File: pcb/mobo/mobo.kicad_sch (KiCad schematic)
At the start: 66 parts, among them J1 SWD_10, J2 PEEL_MOTOR, J3 DRIVE_MOTOR, J4 SW1, J5 SPRING_FINGERS, J6 SW2, J7 SW1, J8 USART1, J9 SWD_10, U1 STM32F031C6Tx, U2 STM32F031K6Ux, U4 AP1117-33, U5 MC34063AD, U6 MAX3078E, U7 DRV8837, U8 DRV8837, Y1 8MHz

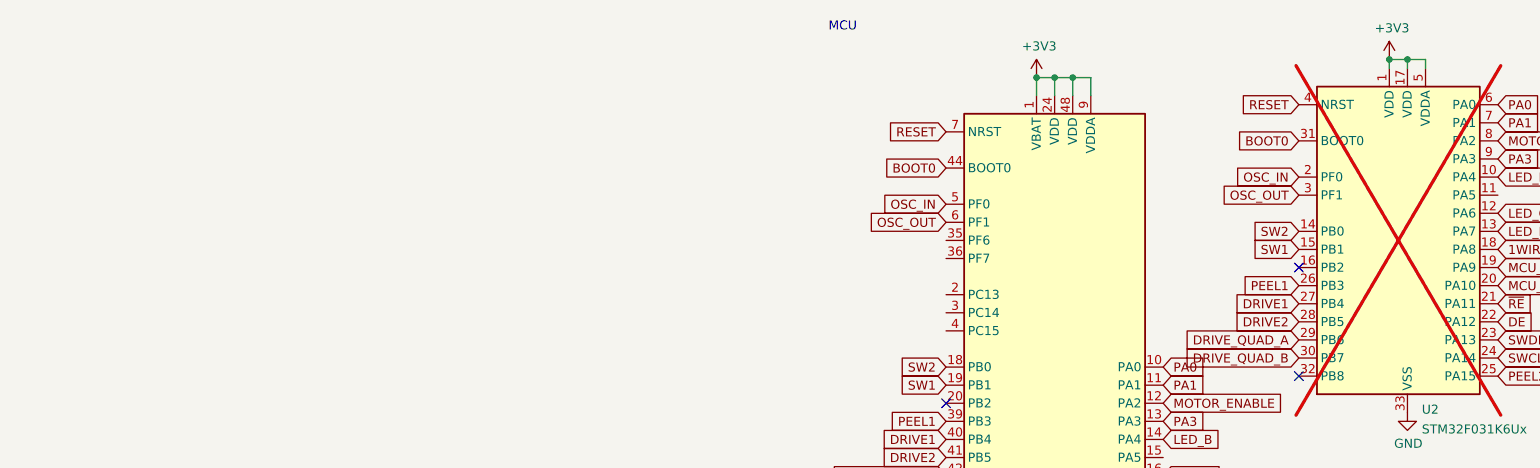
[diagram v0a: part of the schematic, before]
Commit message: Invalid LCSC part for crystal, changed to C527077
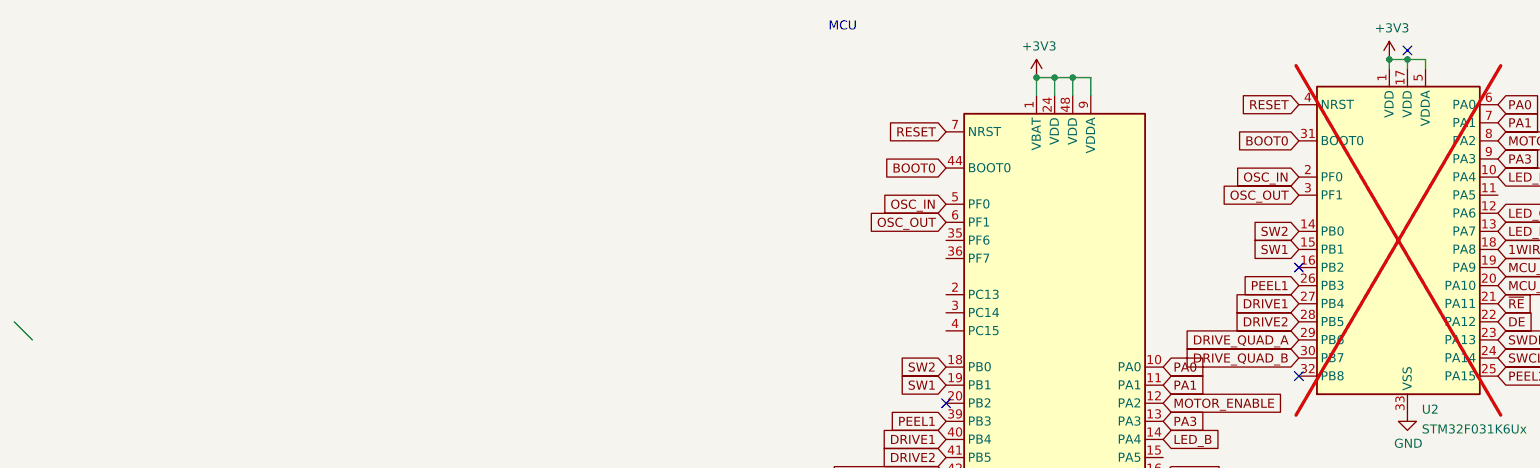
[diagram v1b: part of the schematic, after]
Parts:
- Y1: LCSC C115962 -> C7294546
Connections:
- no-connect marks 8 -> 9
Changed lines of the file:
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@@
 	)
 	(no_connect
+		(at 93.98 17.78)
+	)
+	(no_connect
 		(at 78.74 63.5)
 	)
@@
 		(at 165.1 91.44)
 	)
+	(bus_entry
+		(at -101.6 55.88)
+		(size 2.54 2.54)
+		(stroke
+			(width 0)
+			(type default)
+		)
+	)
 	(wire
 		(pts
@@
 			)
 		)
-		(property "LCSC" "C115962"
+		(property "LCSC" "C7294546"
 			(at 130.81 36.83 0)
 			(effects
@@
 			)
 		)
+		(property "Notes" ""
+			(at 130.81 36.83 0)
+			(effects
+				(font
+					(size 1.27 1.27)
+				)
+				(hide yes)
+			)
+		)
 		(pin "1"
 		)
@@
 			(at 152.4 36.83 0)
 			(effects
+				(font
+					(size 1.27 1.27)
+				)
+				(hide yes)
+			)
+		)
+		(property "DigiKey" ""
+			(at 152.4 36.83 0)
+			(effects

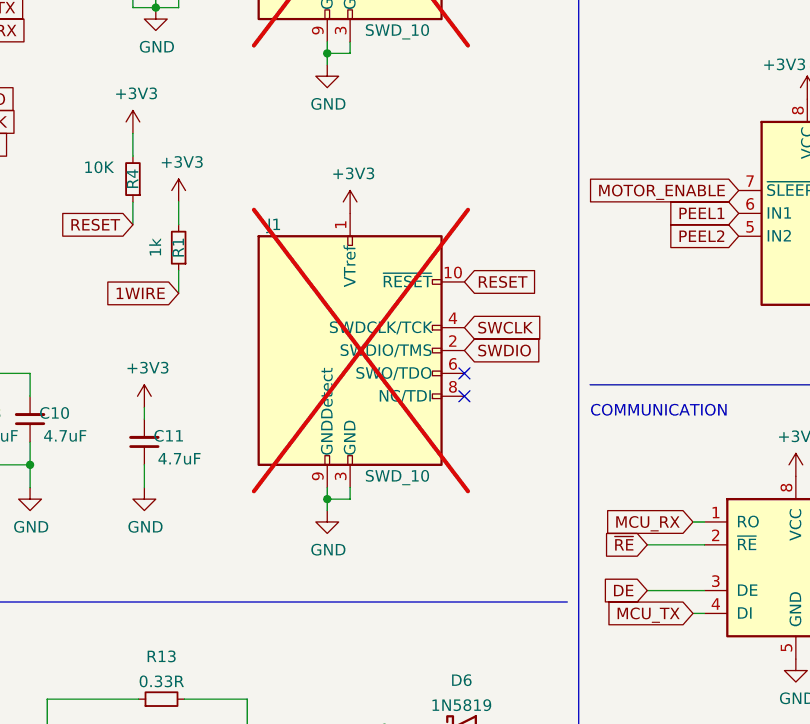
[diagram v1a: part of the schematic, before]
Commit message: Convert SWD connector on back to TC2030. Left one on front for Adafruit 5434 connector.
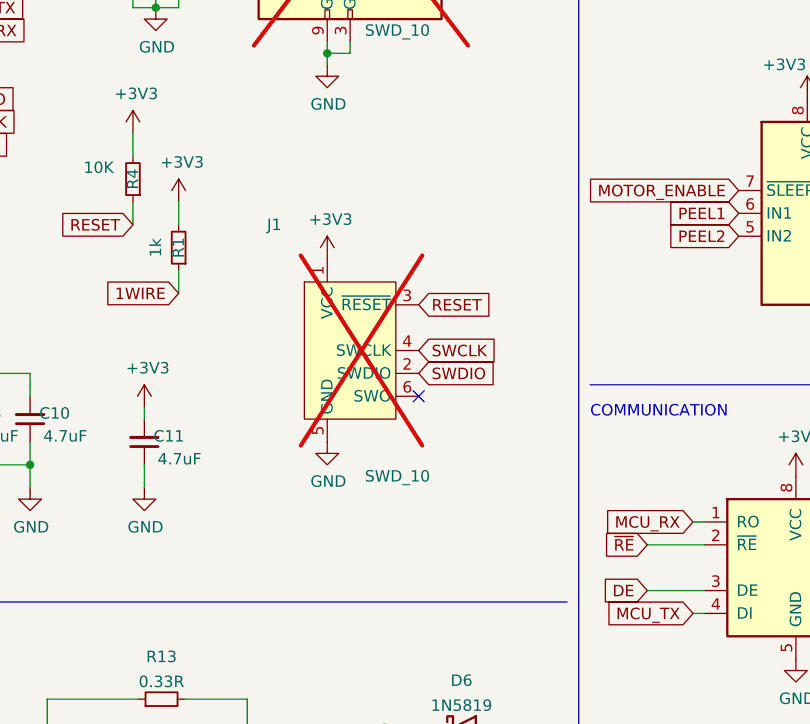
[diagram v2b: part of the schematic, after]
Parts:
- J1: footprint Connector_PinHeader_1.27mm:PinHeader_2x05_P1.27mm_Vertical_SMD -> Connector:Tag-Connect_TC2030-IDC-FP_2x03_P1.27mm_Vertical; symbol Connector:Conn_ARM_JTAG_SWD_10 -> Connector:Conn_ARM_SWD_TagConnect_TC2030; now left out of the parts list
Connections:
- net GND: no longer J1.3 (GND), J1.9 (GNDDetect)
- net RESET: now also J1.3 (~{RESET}); no longer J1.10 (~{RESET})
- no-connect marks 9 -> 8
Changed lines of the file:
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@@
 	)
 	(junction
-		(at 149.86 102.87)
-		(diameter 0)
-		(color 0 0 0 0)
-	)
-	(junction
 		(at 74.93 88.9)
 		(diameter 0)
@@
 	)
 	(no_connect
-		(at 165.1 88.9)
-	)
-	(no_connect
-		(at 165.1 91.44)
+		(at 160.02 91.44)
 	)
 	(bus_entry
@@
 	(wire
 		(pts
-			(xy 152.4 102.87) (xy 152.4 101.6)
-		)
-		(stroke
-			(width 0)
-			(type default)
-		)
-	)
-	(wire
-		(pts
 			(xy 140.97 140.97) (xy 143.51 140.97)
 		)
@@
 	(wire
 		(pts
-			(xy 149.86 102.87) (xy 149.86 101.6)
-		)
-		(stroke
-			(width 0)
-			(type default)
-		)
-	)
-	(wire
-		(pts
 			(xy 109.22 96.52) (xy 109.22 99.06)
 		)
@@
 	(wire
 		(pts
-			(xy 149.86 102.87) (xy 152.4 102.87)
-		)
-		(stroke
-			(width 0)
-			(type default)
-		)
-	)
-	(wire
-		(pts
 			(xy 78.74 180.34) (xy 81.28 180.34)
 		)
@@
 	(wire
 		(pts
-			(xy 149.86 104.14) (xy 149.86 102.87)
-		)
-		(stroke
-			(width 0)
-			(type default)
-		)
-	)
-	(wire
-		(pts
 			(xy 38.1 157.48) (xy 38.1 162.56)
 		)
@@
 	(global_label "SWCLK"
 		(shape input)
-		(at 165.1 83.82 0)
+		(at 160.02 86.36 0)
 		(fields_autoplaced yes)
 		(effects
@@
 		)
 		(property "Intersheetrefs" "${INTERSHEET_REFS}"
-			(at 121.285 1.905 0)
+			(at 116.205 4.445 0)
 			(effects
 				(font
@@
 	(global_label "SWDIO"
 		(shape input)
-		(at 165.1 86.36 0)
+		(at 160.02 88.9 0)
 		(fields_autoplaced yes)
 		(effects
@@
 		)
 		(property "Intersheetrefs" "${INTERSHEET_REFS}"
-			(at 121.285 1.905 0)
+			(at 116.205 4.445 0)
 			(effects
 				(font
@@
 	(global_label "RESET"
 		(shape input)
-		(at 165.1 78.74 0)
+		(at 160.02 81.28 0)
 		(fields_autoplaced yes)
 		(effects
@@
 		)
 		(property "Intersheetrefs" "${INTERSHEET_REFS}"
-			(at 121.285 1.905 0)
+			(at 116.205 4.445 0)
 			(effects
 				(font
@@
 	(symbol
 		(lib_id "power:GND")
-		(at 149.86 104.14 0)
+		(at 149.86 96.52 0)
 		(unit 1)
 		(exclude_from_sim no)
@@
 		(dnp no)
 		(property "Reference" "#PWR04"
-			(at 149.86 110.49 0)
+			(at 149.86 102.87 0)
 			(effects
 				(font
@@
 		)
 		(property "Value" "GND"
-			(at 149.987 108.5342 0)
+			(at 149.987 100.9142 0)
 			(effects
 				(font
@@
 		)
 		(property "Footprint" ""
-			(at 149.86 104.14 0)
+			(at 149.86 96.52 0)
 			(effects
 				(font
@@
 		)
 		(property "Datasheet" ""
-			(at 149.86 104.14 0)
+			(at 149.86 96.52 0)
 			(effects
 				(font
@@
 		)
 		(property "Description" ""
-			(at 149.86 104.14 0)
+			(at 149.86 96.52 0)
 			(effects
 				(font
@@
 	(symbol
 		(lib_id "power:+3V3")
-		(at 152.4 71.12 0)
+		(at 149.86 76.2 0)
 		(unit 1)
 		(exclude_from_sim no)
@@
 		(dnp no)
 		(property "Reference" "#PWR05"
-			(at 152.4 74.93 0)
+			(at 149.86 80.01 0)
 			(effects
 				(font
@@
 		)
 		(property "Value" "+3V3"
-			(at 152.781 66.7258 0)
+			(at 150.241 71.8058 0)
 			(effects
 				(font
@@
 		)
 		(property "Footprint" ""
-			(at 152.4 71.12 0)
+			(at 149.86 76.2 0)
 			(effects
 				(font
@@
 		)
 		(property "Datasheet" ""
-			(at 152.4 71.12 0)
+			(at 149.86 76.2 0)
 			(effects
 				(font
@@
 		)
 		(property "Description" ""
-			(at 152.4 71.12 0)
+			(at 149.86 76.2 0)
 			(effects
 				(font
@@
 	)
 	(symbol
-		(lib_id "Connector:Conn_ARM_JTAG_SWD_10")
+		(lib_id "Connector:Conn_ARM_SWD_TagConnect_TC2030")
 		(at 152.4 86.36 0)
 		(unit 1)
 		(exclude_from_sim no)
-		(in_bom yes)
+		(in_bom no)
 		(on_board yes)
 		(dnp yes)
@@
 			)
 		)
-		(property "Footprint" "Connector_PinHeader_1.27mm:PinHeader_2x05_P1.27mm_Vertical_SMD"
-			(at 152.4 86.36 0)
+		(property "Footprint" "Connector:Tag-Connect_TC2030-IDC-FP_2x03_P1.27mm_Vertical"
+			(at 152.4 104.14 0)
 			(effects
 				(font
@@
 			)
 		)
-		(property "Datasheet" "http://infocenter.arm.com/help/topic/com.arm.doc.ddi0314h/DDI0314H_coresight_components_trm.pdf"
-			(at 143.51 118.11 90)
+		(property "Datasheet" "https://www.tag-connect.com/wp-content/uploads/bsk-pdf-manager/TC2030-CTX_1.pdf"
+			(at 152.4 101.6 0)
 			(effects
 				(font
@@
 			)
 		)
-		(property "Description" ""
+		(property "Description" "Tag-Connect ARM Cortex SWD JTAG connector, 6 pin"
 			(at 152.4 86.36 0)
 			(effects
@@
 			)
 		)
-		(pin "1"
+		(property "LCSC" ""
+			(at 152.4 86.36 0)
+			(effects
+				(font
+					(size 1.27 1.27)
+				)
+				(hide yes)
+			)
 		)
-		(pin "10"
+		(property "DigiKey" ""
+			(at 152.4 86.36 0)
+			(effects
+				(font
+					(size 1.27 1.27)
+				)
+				(hide yes)
+			)
+		)
+		(property "Mouser" ""
+			(at 152.4 86.36 0)
+			(effects
+				(font
+					(size 1.27 1.27)
+				)
+				(hide yes)
+			)
+		)
+		(pin "1"
 		)
 		(pin "2"
@@
 		(pin "6"
 		)
-		(pin "7"
-		)
-		(pin "8"
-		)
-		(pin "9"
-		)
 		(instances
 			(project "mobo"
@@
 			(at 152.4 36.83 0)
 			(effects
+				(font
+					(size 1.27 1.27)
+				)
+				(hide yes)
+			)
+		)
+		(property "LCSC" ""
+			(at 152.4 36.83 0)
+			(effects
+				(font
+					(size 1.27 1.27)
+				)
+				(hide yes)
+			)
+		)
+		(property "Mouser" ""
+			(at 152.4 36.83 0)
+			(effects

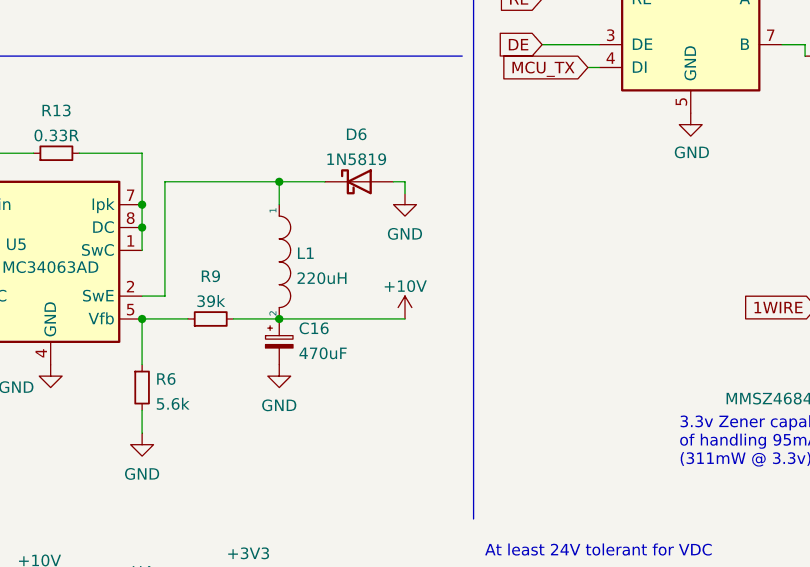
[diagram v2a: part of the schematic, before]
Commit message: Modify SWD footprint to make compatible with Adafruit 5434
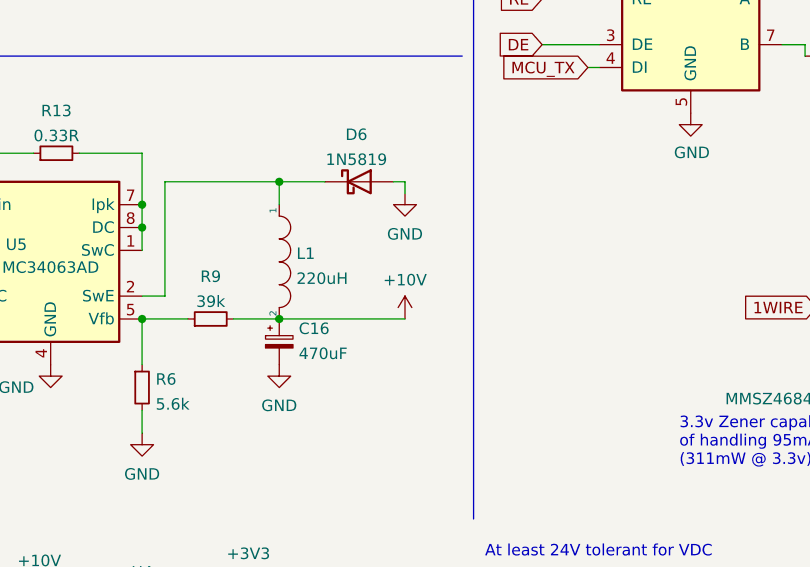
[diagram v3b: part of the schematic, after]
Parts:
- C12: DigiKey 565-EMZR500ARA101MF80GCT-ND -> PCE3951CT-ND; LCSC C962164 -> C178512; Mouser 661-EMZR500ARA101MF8 -> 667-EEE-1VA101XP
- D6: footprint Diode_SMD:D_SOD-123 -> Diode_SMD:D_SOD-323_HandSoldering; LCSC C963381 -> C191023
- J2: DigiKey WM1746-ND -> WM7620CT-ND; Mouser 538-53048-0610 -> 53261-0271; Notes MouserAlt: 53261-0671; DigiKeyAlt: WM7624CT-ND -> Order cable ‎0151340201, it's female to female 100mm. Cut i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
- J3: Notes MouserAlt: 53261-0671; DigiKeyAlt: WM7624CT-ND -> (none)
- J9: DigiKey (none) -> 1528-5434-ND; Mouser (none) -> 485-5434; Notes WARNING: Is there room in the model for this -> Adafruit 5434 compatible; now left out of the parts list
- Y1: LCSC C7294546 -> C5308002
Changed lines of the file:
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@@
 			)
 		)
-		(property "LCSC" "C7294546"
+		(property "LCSC" "C5308002"
 			(at 130.81 36.83 0)
 			(effects
@@
 			)
 		)
+		(property "Notes" ""
+			(at 201.93 110.49 0)
+			(effects
+				(font
+					(size 1.27 1.27)
+				)
+				(hide yes)
+			)
+		)
 		(pin "1"
 		)
@@
 		(unit 1)
 		(exclude_from_sim no)
-		(in_bom yes)
+		(in_bom no)
 		(on_board yes)
 		(dnp yes)
@@
 			)
 		)
-		(property "Description" ""
+		(property "Description" "2x5p 1.27mm Pogo"
 			(at 152.4 36.83 0)
 			(effects
@@
 			)
 		)
-		(property "Notes" "WARNING: Is there room in the model for this"
+		(property "Notes" "Adafruit 5434 compatible"
 			(at 152.4 36.83 0)
 			(effects
@@
 			)
 		)
-		(property "DigiKey" ""
+		(property "DigiKey" "1528-5434-ND"
 			(at 152.4 36.83 0)
 			(effects
@@
 			)
 		)
-		(property "Mouser" ""
+		(property "Mouser" "485-5434"
 			(at 152.4 36.83 0)
 			(effects
@@
 			)
 		)
-		(property "Description" ""
+		(property "Description" "100V X5R"
 			(at 116.84 144.78 0)
 			(effects
@@
 			)
 		)
-		(property "Footprint" "Diode_SMD:D_SOD-123"
+		(property "Footprint" "Diode_SMD:D_SOD-323_HandSoldering"
 			(at 165.1 132.715 0)
 			(effects
@@
 			)
 		)
-		(property "LCSC" "C963381"
+		(property "LCSC" "C191023"
 			(at 165.1 128.27 0)
 			(effects
@@
 			)
 		)
+		(property "Notes" ""
+			(at 165.1 128.27 0)
+			(effects
+				(font
+					(size 1.27 1.27)
+				)
+				(hide yes)
+			)
+		)
 		(pin "1"
 		)
@@
 			)
 		)
-		(property "Description" "PicoBlade 1x6 right-angle Header"
+		(property "Description" "PicoBlade 1x2 right-angle Header"
 			(at 234.95 73.66 0)
 			(effects
@@
 			)
 		)
-		(property "DigiKey" "WM1746-ND"
+		(property "DigiKey" "WM7620CT-ND"
 			(at 234.95 73.66 0)
 			(effects
@@
 			)
 		)
-		(property "Mouser" "538-53048-0610"
+		(property "Mouser" "53261-0271"
 			(at 234.95 73.66 0)
 			(effects
@@
 			)
 		)
-		(property "Notes" "MouserAlt: 53261-0671; DigiKeyAlt: WM7624CT-ND"
+		(property "Notes" "Order cable ‎0151340201, it's female to female 100mm. Cut in half, makes two peel motor pigtails"
 			(at 234.95 73.66 0)
 			(effects
@@
 		(on_board yes)
 		(dnp no)
-		(fields_autoplaced yes)
 		(property "Reference" "#PWR0114"
 			(at 170.18 147.32 0)
@@
 		)
 		(property "Value" "+10V"
-			(at 170.18 139.9055 0)
+			(at 170.18 139.192 0)
 			(effects
 				(font
@@
 			)
 		)
-		(property "Notes" "MouserAlt: 53261-0671; DigiKeyAlt: WM7624CT-ND"
+		(property "Notes" ""
 			(at 242.57 27.94 0)
 			(effects
@@
 			)
 		)
-		(property "Description" "100uf 50V 2000H@105c ±20%"
+		(property "Description" "100uf 35V 2000H@105c ±20%"
 			(at 110.49 133.35 0)
 			(effects
@@
 			)
 		)
-		(property "LCSC" "C962164"
+		(property "LCSC" "C178512"
 			(at 110.49 133.35 0)
 			(effects
@@
 			)
 		)
-		(property "DigiKey" "565-EMZR500ARA101MF80GCT-ND"
+		(property "DigiKey" "PCE3951CT-ND"
 			(at 110.49 133.35 0)
 			(effects
@@
 			)
 		)
-		(property "Mouser" "661-EMZR500ARA101MF8"
+		(property "Mouser" "667-EEE-1VA101XP"
+			(at 110.49 133.35 0)
+			(effects
+				(font
+					(size 1.27 1.27)
+				)
+				(hide yes)
+			)
+		)
+		(property "Notes" ""
 			(at 110.49 133.35 0)
 			(effects
